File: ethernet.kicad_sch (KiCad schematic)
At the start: 35 parts, among them J3 TE_1888250-1, T1 H1102, U4 MCIMX6Y2DVM09AB, U8 LAN8700C-AEZG

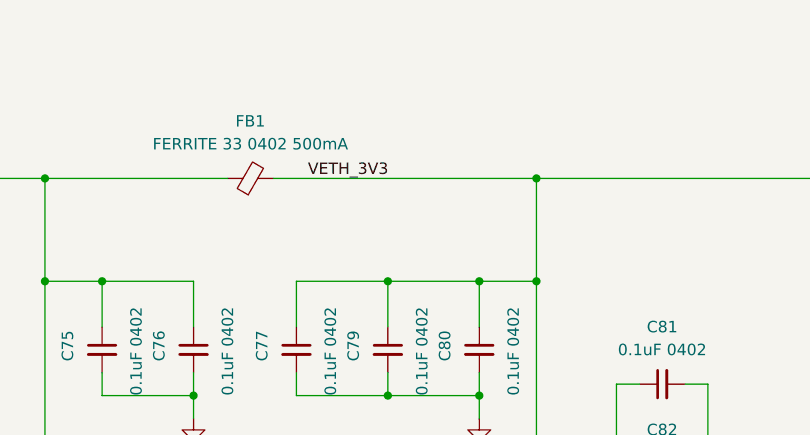
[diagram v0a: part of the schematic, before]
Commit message: ERC: power flags
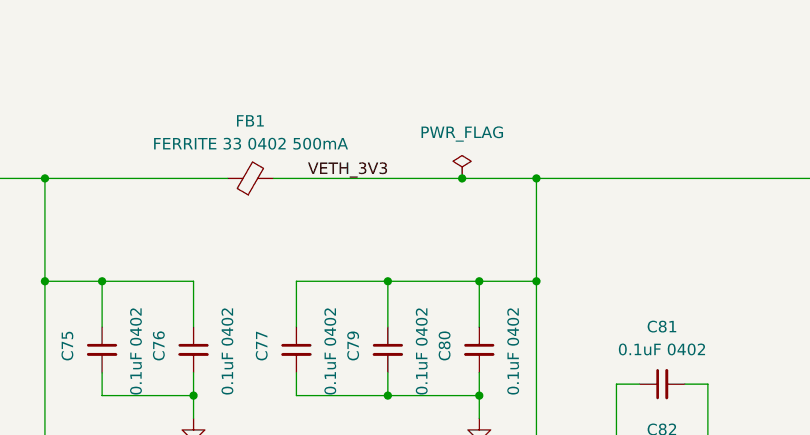
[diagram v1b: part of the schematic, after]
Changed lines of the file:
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@@
   (junction (at 195.58 104.14) (diameter 0) (color 0 0 0 0)
+  )
+  (junction (at 178.435 69.85) (diameter 0) (color 0 0 0 0)
   )
   (junction (at 172.72 107.95) (diameter 0) (color 0 0 0 0)
@@
     (stroke (width 0) (type default) (color 0 0 0 0))
   )
+  (wire (pts (xy 178.435 69.85) (xy 186.69 69.85))
+    (stroke (width 0) (type default) (color 0 0 0 0))
+  )
   (wire (pts (xy 152.4 69.85) (xy 132.08 69.85))
     (stroke (width 0) (type default) (color 0 0 0 0))
@@
     (stroke (width 0) (type default) (color 0 0 0 0))
   )
-  (wire (pts (xy 157.48 69.85) (xy 186.69 69.85))
+  (wire (pts (xy 157.48 69.85) (xy 178.435 69.85))
     (stroke (width 0) (type default) (color 0 0 0 0))
   )
@@
       (effects (font (size 1.27 1.27)) hide)
     )
+    (pin "1")
+  )
+  (symbol (lib_id "power:PWR_FLAG") (at 178.435 69.85 0) (unit 1)
+    (in_bom yes) (on_board yes) (fields_autoplaced)
+    (property "Reference" "#FLG0102" (id 0) (at 178.435 67.945 0)
+      (effects (font (size 1.27 1.27)) hide)
+    )
+    (property "Value" "PWR_FLAG" (id 1) (at 178.435 64.77 0))
+    (property "Footprint" "" (id 2) (at 178.435 69.85 0)
+      (effects (font (size 1.27 1.27)) hide)
+    )
+    (property "Datasheet" "~" (id 3) (at 178.435 69.85 0)
+      (effects (font (size 1.27 1.27)) hide)
+    )

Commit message: Update symbols
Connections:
- net VDD33A renamed VETH_3V3
- now unconnected: T1.12 (NC), T1.13 (NC), T1.4 (NC), T1.5 (NC)

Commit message: Change DDR NC electrical type to Passive so they can be connected
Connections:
- no-connect marks 19 -> 18
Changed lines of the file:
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@@
   (no_connect (at 66.04 138.43))
   (no_connect (at 156.21 156.21))
-  (no_connect (at 303.53 152.4))
   (no_connect (at 156.21 129.54))
   (no_connect (at 66.04 146.05))

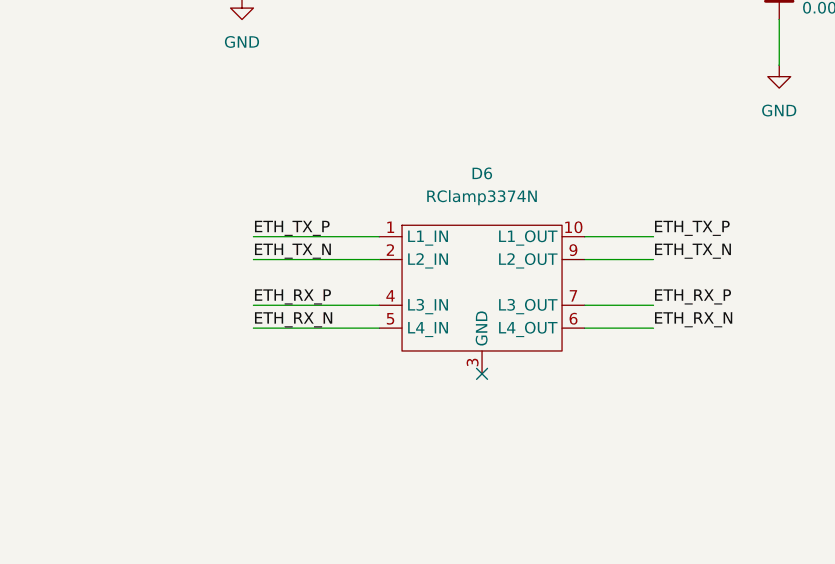
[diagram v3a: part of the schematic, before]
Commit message: Fix NAND and RClamp3374N footprints; ERC
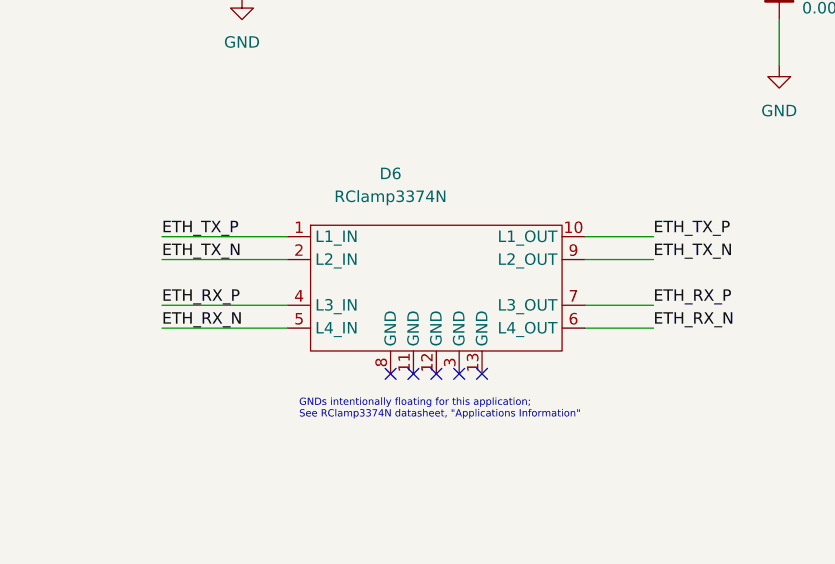
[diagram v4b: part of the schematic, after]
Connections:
- net GND: no longer D6.11 (GND), D6.12 (GND), D6.13 (GND), D6.3 (GND), D6.8 (GND)
- no-connect marks 18 -> 22
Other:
- note added: "GNDs intentionally floating for this application; See RClamp3374N datasheet, "Applications Information""
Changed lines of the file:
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@@
   (no_connect (at 66.04 156.21))
   (no_connect (at 66.04 148.59))
-  (no_connect (at 322.58 212.09))
+  (no_connect (at 312.42 212.09))
   (no_connect (at 177.8 173.99))
+  (no_connect (at 320.04 212.09))
+  (no_connect (at 314.96 212.09))
   (no_connect (at 214.63 161.29))
   (no_connect (at 156.21 147.32))
@@
   (no_connect (at 156.21 163.83))
   (no_connect (at 66.04 153.67))
+  (no_connect (at 317.5 212.09))
+  (no_connect (at 322.58 212.09))
   (wire (pts (xy 138.43 91.44) (xy 138.43 93.98))
     (stroke (width 0) (type default) (color 0 0 0 0))
@@
     (stroke (width 0) (type default) (color 0 0 0 0))
   )
-  (wire (pts (xy 297.18 199.39) (xy 311.15 199.39))
+  (wire (pts (xy 287.02 199.39) (xy 300.99 199.39))
     (stroke (width 0) (type default) (color 0 0 0 0))
   )
@@
     (stroke (width 0) (type default) (color 0 0 0 0))
   )
-  (wire (pts (xy 297.18 204.47) (xy 311.15 204.47))
+  (wire (pts (xy 287.02 204.47) (xy 300.99 204.47))
     (stroke (width 0) (type default) (color 0 0 0 0))
   )
@@
     (stroke (width 0) (type default) (color 0 0 0 0))
   )
-  (wire (pts (xy 297.18 196.85) (xy 311.15 196.85))
+  (wire (pts (xy 287.02 196.85) (xy 300.99 196.85))
     (stroke (width 0) (type default) (color 0 0 0 0))
   )
@@
     (stroke (width 0) (type default) (color 0 0 0 0))
   )
-  (wire (pts (xy 297.18 207.01) (xy 311.15 207.01))
+  (wire (pts (xy 287.02 207.01) (xy 300.99 207.01))
     (stroke (width 0) (type default) (color 0 0 0 0))
   )
@@
     (stroke (width 0) (type default) (color 0 0 0 0))
   )
+  (text "GNDs intentionally floating for this application;\nSee RClamp3374N datasheet, \"Applications Information\""
+    (at 302.26 217.17 0)
+    (effects (font (size 0.8 0.8)) (justify left bottom))
+  )
   (text "COL/RMII/CRS_DV pulled\nup for RMII mode" (at 77.47 110.49 0)
     (effects (font (size 1.27 1.27)) (justify left bottom))
@@
     (effects (font (size 1.27 1.27)) (justify left bottom))
   )
-  (label "ETH_RX_P" (at 297.18 204.47 0)
+  (label "ETH_RX_P" (at 287.02 204.47 0)
     (effects (font (size 1.27 1.27)) (justify left bottom))
   )
@@
     (effects (font (size 1.27 1.27)) (justify left bottom))
   )
-  (label "ETH_TX_N" (at 297.18 199.39 0)
-    (effects (font (size 1.27 1.27)) (justify left bottom))
-  )
-  (label "ETH_RX_N" (at 297.18 207.01 0)
-    (effects (font (size 1.27 1.27)) (justify left bottom))
-  )
-  (label "ETH_TX_P" (at 297.18 196.85 0)
+  (label "ETH_TX_N" (at 287.02 199.39 0)
+    (effects (font (size 1.27 1.27)) (justify left bottom))
+  )
+  (label "ETH_RX_N" (at 287.02 207.01 0)
+    (effects (font (size 1.27 1.27)) (justify left bottom))
+  )
+  (label "ETH_TX_P" (at 287.02 196.85 0)
     (effects (font (size 1.27 1.27)) (justify left bottom))
   )
@@
     (pin "2")
   )
-  (symbol (lib_id "catfood:RClamp3374N") (at 331.47 201.93 0) (unit 1)
+  (symbol (lib_id "catfood:RClamp3374N") (at 321.31 201.93 0) (unit 1)
     (in_bom yes) (on_board yes) (fields_autoplaced)
-    (property "Reference" "D6" (id 0) (at 322.58 189.865 0))
-    (property "Value" "RClamp3374N" (id 1) (at 322.58 192.405 0))
-    (property "Footprint" "" (id 2) (at 331.47 201.93 0)
-      (effects (font (size 1.27 1.27)) hide)
-    )
-    (property "Datasheet" "" (id 3) (at 331.47 201.93 0)
-      (effects (font (size 1.27 1.27)) hide)
-    )
+    (property "Reference" "D6" (id 0) (at 312.42 189.865 0))
+    (property "Value" "RClamp3374N" (id 1) (at 312.42 192.405 0))
+    (property "Footprint" "" (id 2) (at 321.31 201.93 0)
+      (effects (font (size 1.27 1.27)) hide)
+    )
+    (property "Datasheet" "" (id 3) (at 321.31 201.93 0)
+      (effects (font (size 1.27 1.27)) hide)
+    )

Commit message: Footprint assignments for standard passives
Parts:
- C74, C75, C76, C77, C78, C79, C80, C81, C83, C84: footprint (none) -> Capacitor_SMD:C_0402_1005Metric
- C82: footprint (none) -> Capacitor_SMD:C_0603_1608Metric
- R27, R28, R29, R30, R31, R32, R33, R34, R35, R36, R37, R38, R39, R40, R41, R42, R43: footprint (none) -> Resistor_SMD:R_0402_1005Metric
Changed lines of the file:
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@@
       (effects (font (size 1.27 1.27)) (justify left))
     )
-    (property "Footprint" "" (id 2) (at 198.12 218.44 0)
+    (property "Footprint" "Resistor_SMD:R_0402_1005Metric" (id 2) (at 198.12 218.44 0)
       (effects (font (size 1.27 1.27)) hide)
     )
@@
       (effects (font (size 1.27 1.27)) (justify left))
     )
-    (property "Footprint" "" (id 2) (at 160.02 190.5 0)
+    (property "Footprint" "Capacitor_SMD:C_0402_1005Metric" (id 2) (at 160.02 190.5 0)
       (effects (font (size 1.27 1.27)) hide)
     )
@@
       (effects (font (size 1.27 1.27)) (justify left))
     )
-    (property "Footprint" "" (id 2) (at 105.41 109.22 0)
+    (property "Footprint" "Resistor_SMD:R_0402_1005Metric" (id 2) (at 105.41 109.22 0)
       (effects (font (size 1.27 1.27)) hide)
     )
@@
       (effects (font (size 1.27 1.27)) (justify left))
     )
-    (property "Footprint" "" (id 2) (at 280.67 113.03 0)
+    (property "Footprint" "Resistor_SMD:R_0402_1005Metric" (id 2) (at 280.67 113.03 0)
       (effects (font (size 1.27 1.27)) hide)
     )
@@
       (effects (font (size 1.27 1.27)) (justify left))
     )
-    (property "Footprint" "" (id 2) (at 295.91 163.83 0)
+    (property "Footprint" "Capacitor_SMD:C_0402_1005Metric" (id 2) (at 295.91 163.83 0)
       (effects (font (size 1.27 1.27)) hide)
     )
@@
       (effects (font (size 1.27 1.27)) (justify left))
     )
-    (property "Footprint" "" (id 2) (at 170.18 88.9 0)
+    (property "Footprint" "Capacitor_SMD:C_0402_1005Metric" (id 2) (at 170.18 88.9 0)
       (effects (font (size 1.27 1.27)) hide)
     )
@@
     (property "Reference" "C81" (id 0) (at 200.6663 86.36 90))
     (property "Value" "0.1uF 0402" (id 1) (at 200.6663 88.9 90))
-    (property "Footprint" "" (id 2) (at 200.66 92.71 0)
+    (property "Footprint" "Capacitor_SMD:C_0402_1005Metric" (id 2) (at 200.66 92.71 0)
       (effects (font (size 1.27 1.27)) hide)
     )
@@
       (effects (font (size 1.27 1.27)) (justify left))
     )
-    (property "Footprint" "" (id 2) (at 16.51 118.11 0)
+    (property "Footprint" "Capacitor_SMD:C_0402_1005Metric" (id 2) (at 16.51 118.11 0)
       (effects (font (size 1.27 1.27)) hide)
     )
@@
       (effects (font (size 1.27 1.27)) (justify left))
     )
-    (property "Footprint" "" (id 2) (at 120.65 109.22 0)
+    (property "Footprint" "Resistor_SMD:R_0402_1005Metric" (id 2) (at 120.65 109.22 0)
       (effects (font (size 1.27 1.27)) hide)
     )
@@
     (property "Reference" "C82" (id 0) (at 200.6663 97.79 90))
     (property "Value" "4.7uF 0603" (id 1) (at 200.6663 100.33 90))
-    (property "Footprint" "" (id 2) (at 200.66 104.14 0)
+    (property "Footprint" "Capacitor_SMD:C_0603_1608Metric" (id 2) (at 200.66 104.14 0)
       (effects (font (size 1.27 1.27)) hide)
     )
@@
       (effects (font (size 1.27 1.27)) (justify left))
     )
-    (property "Footprint" "" (id 2) (at 148.59 88.9 0)
+    (property "Footprint" "Capacitor_SMD:C_0402_1005Metric" (id 2) (at 148.59 88.9 0)
       (effects (font (size 1.27 1.27)) hide)
     )
@@
       (effects (font (size 1.27 1.27)) (justify left))
     )
-    (property "Footprint" "" (id 2) (at 222.25 196.85 0)
+    (property "Footprint" "Capacitor_SMD:C_0402_1005Metric" (id 2) (at 222.25 196.85 0)
       (effects (font (size 1.27 1.27)) hide)
     )
@@
     (property "Reference" "R38" (id 0) (at 350.52 149.86 90))
     (property "Value" "75R 0402" (id 1) (at 350.52 154.94 90))
-    (property "Footprint" "" (id 2) (at 350.52 152.4 0)
+    (property "Footprint" "Resistor_SMD:R_0402_1005Metric" (id 2) (at 350.52 152.4 0)
       (effects (font (size 1.27 1.27)) hide)
     )
@@
     (property "Reference" "R41" (id 0) (at 361.95 157.48 90))
     (property "Value" "75R 0402" (id 1) (at 361.95 162.56 90))
-    (property "Footprint" "" (id 2) (at 361.95 160.02 0)
+    (property "Footprint" "Resistor_SMD:R_0402_1005Metric" (id 2) (at 361.95 160.02 0)
       (effects (font (size 1.27 1.27)) hide)
     )
@@
       (effects (font (size 1.27 1.27)) (justify left))
     )
-    (property "Footprint" "" (id 2) (at 138.43 88.9 0)
+    (property "Footprint" "Capacitor_SMD:C_0402_1005Metric" (id 2) (at 138.43 88.9 0)
       (effects (font (size 1.27 1.27)) hide)
     )
@@
     (property "Reference" "R42" (id 0) (at 387.35 120.65 90))
     (property "Value" "330R 0402" (id 1) (at 394.97 120.65 90))
-    (property "Footprint" "" (id 2) (at 392.43 123.19 0)
+    (property "Footprint" "Resistor_SMD:R_0402_1005Metric" (id 2) (at 392.43 123.19 0)
       (effects (font (size 1.27 1.27)) hide)
     )
@@
       (effects (font (size 1.27 1.27)) (justify left))
     )
-    (property "Footprint" "" (id 2) (at 180.34 205.74 0)
+    (property "Footprint" "Resistor_SMD:R_0402_1005Metric" (id 2) (at 180.34 205.74 0)
       (effects (font (size 1.27 1.27)) hide)
     )
@@
       (effects (font (size 1.27 1.27)) (justify left))
     )
-    (property "Footprint" "" (id 2) (at 222.25 184.15 0)
+    (property "Footprint" "Resistor_SMD:R_0402_1005Metric" (id 2) (at 222.25 184.15 0)
       (effects (font (size 1.27 1.27)) hide)
     )
@@
     (property "Reference" "R29" (id 0) (at 153.67 180.34 90))
     (property "Value" "10R 0402" (id 1) (at 154.94 185.42 90))
-    (property "Footprint" "" (id 2) (at 154.94 182.88 0)
+    (property "Footprint" "Resistor_SMD:R_0402_1005Metric" (id 2) (at 154.94 182.88 0)
       (effects (font (size 1.27 1.27)) hide)
     )
@@
     (property "Reference" "R43" (id 0) (at 387.35 151.13 90))
     (property "Value" "330R 0402" (id 1) (at 394.97 151.13 90))
-    (property "Footprint" "" (id 2) (at 392.43 153.67 0)
+    (property "Footprint" "Resistor_SMD:R_0402_1005Metric" (id 2) (at 392.43 153.67 0)
       (effects (font (size 1.27 1.27)) hide)
     )
@@
     (property "Reference" "R39" (id 0) (at 350.52 157.48 90))
     (property "Value" "75R 0402" (id 1) (at 350.52 162.56 90))
-    (property "Footprint" "" (id 2) (at 350.52 160.02 0)
+    (property "Footprint" "Resistor_SMD:R_0402_1005Metric" (id 2) (at 350.52 160.02 0)
       (effects (font (size 1.27 1.27)) hide)
     )
@@
       (effects (font (size 1.27 1.27)) (justify left))
     )
-    (property "Footprint" "" (id 2) (at 295.91 113.03 0)
+    (property "Footprint" "Resistor_SMD:R_0402_1005Metric" (id 2) (at 295.91 113.03 0)
       (effects (font (size 1.27 1.27)) hide)
     )
@@
     (property "Reference" "R40" (id 0) (at 361.95 149.86 90))
     (property "Value" "75R 0402" (id 1) (at 361.95 154.94 90))
-    (property "Footprint" "" (id 2) (at 361.95 152.4 0)
+    (property "Footprint" "Resistor_SMD:R_0402_1005Metric" (id 2) (at 361.95 152.4 0)
       (effects (font (size 1.27 1.27)) hide)
     )
@@
       (effects (font (size 1.27 1.27)) (justify left))
     )
-    (property "Footprint" "" (id 2) (at 160.02 88.9 0)
+    (property "Footprint" "Capacitor_SMD:C_0402_1005Metric" (id 2) (at 160.02 88.9 0)
       (effects (font (size 1.27 1.27)) hide)
     )
@@
       (effects (font (size 1.27 1.27)) (justify left))
     )
-    (property "Footprint" "" (id 2) (at 250.19 113.03 0)
+    (property "Footprint" "Resistor_SMD:R_0402_1005Metric" (id 2) (at 250.19 113.03 0)
       (effects (font (size 1.27 1.27)) hide)
     )
@@
       (effects (font (size 1.27 1.27)) (justify left))
     )
-    (property "Footprint" "" (id 2) (at 180.34 88.9 0)
+    (property "Footprint" "Capacitor_SMD:C_0402_1005Metric" (id 2) (at 180.34 88.9 0)
       (effects (font (size 1.27 1.27)) hide)
     )
@@
       (effects (font (size 1.27 1.27)) (justify left))
     )
-    (property "Footprint" "" (id 2) (at 265.43 113.03 0)
+    (property "Footprint" "Resistor_SMD:R_0402_1005Metric" (id 2) (at 265.43 113.03 0)
       (effects (font (size 1.27 1.27)) hide)
     )
@@
       (effects (font (size 1.27 1.27)) (justify left))
     )
-    (property "Footprint" "" (id 2) (at 234.95 113.03 0)
-      (effects (font (size 1.27 1.27)) hide)
-    )
+    (property "Footprint" "Resistor_SMD:R_0402_1005Metric" (id 2) (at 234.95 113.03 0)
+      (effects (font (size 1.27 1.27)) hide)
+    )
